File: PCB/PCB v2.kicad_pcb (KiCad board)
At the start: 4 copper layers, 56 x 45 mm, 132 parts, among them J2 USB_C_Receptacle_PowerOnly_6P, J3 6871XX182122_687110182122, J5 Conn_01x03_Pin, J7 Conn_02x06_Odd_Even, U1 TPD2E2U06DCK, U11 OPA4350EA_250, U12 OPA4350EA_250, U13 OPA4350EA_250, U2 ADS131M08xPBS, U3 74LVC1G17, U4 LM27762, U6 OPA4350EA_250, U7 LP5907MFX-3.3

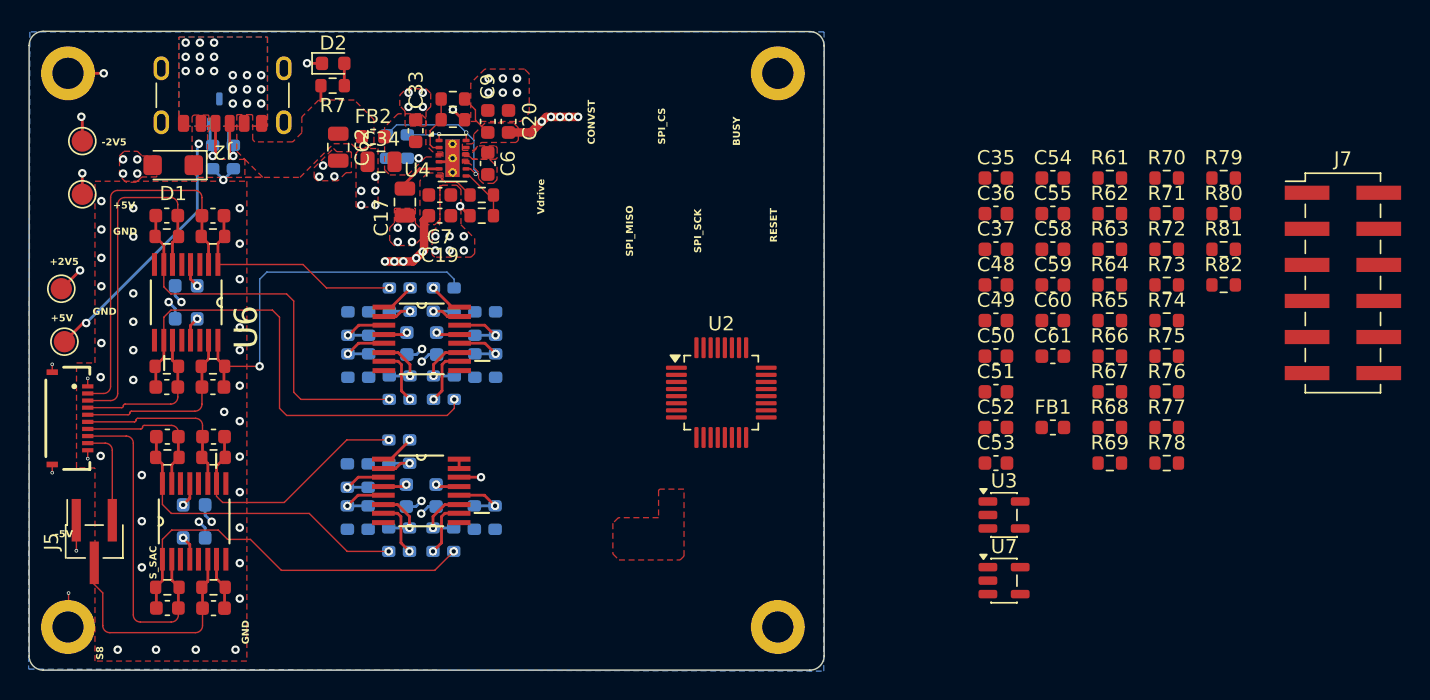
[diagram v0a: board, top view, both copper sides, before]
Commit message: Place U2, J7 and the ADC input dividers in a staggered two-column block
Placed in pcbnew:
- U2 (ADS131M08) at (166.74, 102.07).
- J7 (MCU header) at (165.03, 87.18), rotated -90.
- The Vout1 divider group, a vertical stack of C48 / R61 / R62 at
  x 156.08:
  - the 10 nF and the 1 kOhm to GND tie to the 1.1 kOhm's AIN pad;
  - the Vout pad sits between the two GND pads;
  - Vout1 is routed from U11, and the AIN0P spine is in place.

The other seven groups (R63-R76, C49-C55) copy that group shape exactly.
Eight 3.9 mm stacks in one column would need about 35 mm, and only
about 28 mm is free between J7 and the bottom edge. So they sit in two
columns, staggered by half a pitch:
- Column A at x 156.08: R61, R65, R69, R73 (AIN0/2/4/6).
- Column B at x 159.28: R63, R67, R71, R75 (AIN1/3/5/7).
- Group pitch is 4.7 mm, and column B is offset by 2.35 mm.

How the stagger works:
- Each column-B Vout enters straight through a gap in column A, between
  two GND pads.
- Each column-A AIN output leaves straight through a gap in column B.
- The groups run top to bottom in AIN0-7 order, so the fan-in to U2's
  top, left and bottom pins has no crossings.
- The block spans x 154.8-160.5 and y 91.9-112.2, leaving about 2.3 mm
  to U2's left pins.

Each group's AIN connections are routed like the Vout1 group
(0.1 mm, F.Cu).

DRC:
- Unconnected items 117 -> 103.
- No copper or courtyard violations added. The C48/J7 courtyard overlap
  comes from the manual placement.
- 40 new silkscreen reference overlaps, because the block is dense; this
  is cosmetic.

Still open: the GND pads of the divider block are not connected yet
(needs vias or an F.Cu GND pour).

Co-Authored-By: Claude Opus 5.5 <noreply@anthropic.com>
Claude-Session: https://claude.ai/code/session_01FkMyFfAWNWvsXoQ2tBz5gZ
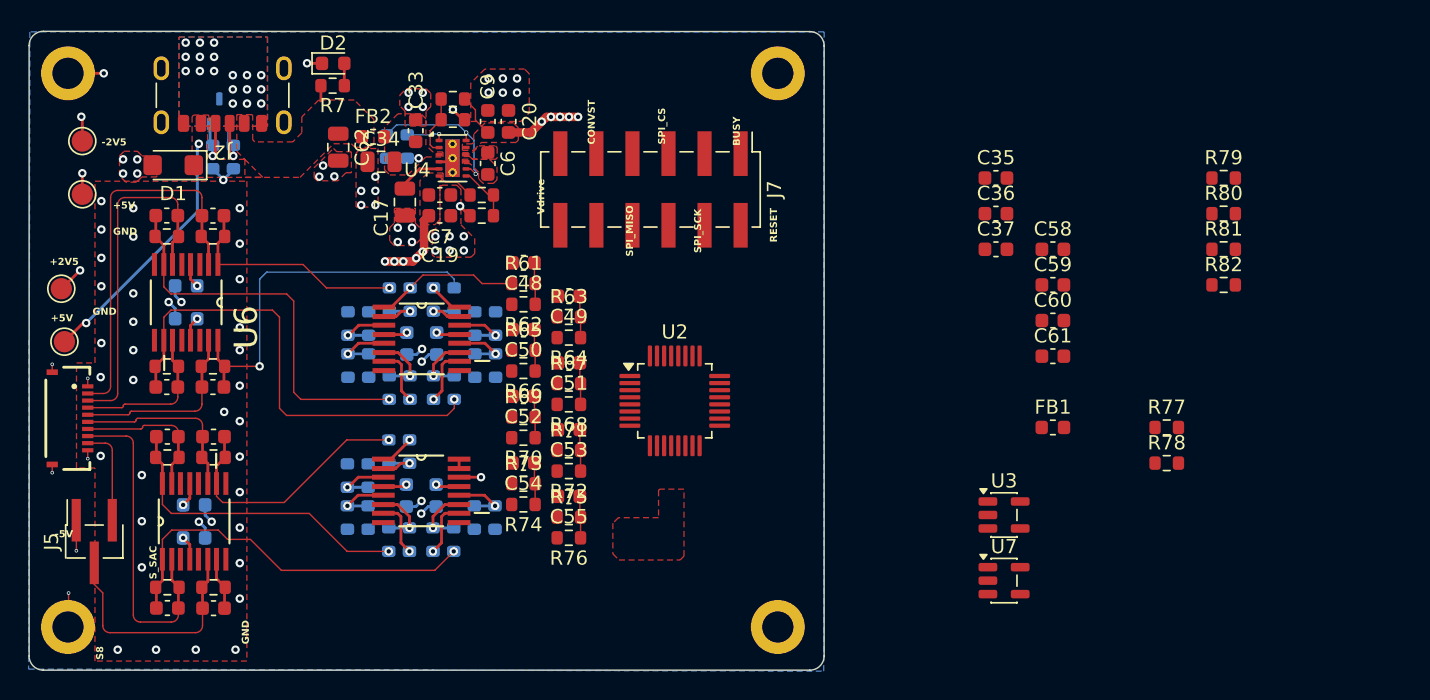
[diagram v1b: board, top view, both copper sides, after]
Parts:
- moved J7 49.2 mm to (165.0, 87.2), turned to -90 degrees
- moved R70 48.9 mm to (156.1, 104.7), turned to 180 degrees
- moved R73 47.4 mm to (156.1, 107.9)
- moved R74 47.1 mm to (156.1, 109.4), turned to 180 degrees
- moved R71 45.3 mm to (159.3, 105.6)
- moved R72 44.9 mm to (159.3, 107.0), turned to 180 degrees
- moved R75 43.6 mm to (159.3, 110.3)
- moved R76 43.4 mm to (159.3, 111.7), turned to 180 degrees
- moved C54 42.4 mm to (156.1, 106.4), turned to 180 degrees
- moved R61 42.0 mm to (156.1, 93.8)
- moved R62 41.8 mm to (156.1, 95.3), turned to 180 degrees
- moved R69 41.4 mm to (156.1, 103.2)
- moved R65 41.4 mm to (156.1, 98.5)
- moved R66 41.3 mm to (156.1, 100.0), turned to 180 degrees
- moved C55 39.5 mm to (159.3, 108.8), turned to 180 degrees
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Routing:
- net Vout1: track 2.43 -> 10.2 mm
- net /POWER SUPPLY - ADC - SACRIFIED SENSOR/AIN0P: track 0.00 -> 2.95 mm
- net /POWER SUPPLY - ADC - SACRIFIED SENSOR/AIN6P: track 0.00 -> 2.93 mm
- net /POWER SUPPLY - ADC - SACRIFIED SENSOR/AIN1P: track 0.00 -> 2.93 mm
- net /POWER SUPPLY - ADC - SACRIFIED SENSOR/AIN7P: track 0.00 -> 2.92 mm
- net /POWER SUPPLY - ADC - SACRIFIED SENSOR/AIN5P: track 0.00 -> 2.92 mm
- net /POWER SUPPLY - ADC - SACRIFIED SENSOR/AIN4P: track 0.00 -> 2.92 mm
- net /POWER SUPPLY - ADC - SACRIFIED SENSOR/AIN3P: track 0.00 -> 2.92 mm
- net /POWER SUPPLY - ADC - SACRIFIED SENSOR/AIN2P: track 0.00 -> 2.92 mm

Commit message: Route the ADC fan-in and Vout5-Vout7 to their dividers
AIN0P-AIN7P fan-in (routed in pcbnew, 0.1 mm, F.Cu):
- Each group's AIN spine runs to its U2 pin with no crossings.
- AIN0/1 go to the top pins, AIN2-5 to the left side, AIN6/7 to the
  bottom.

U12 outputs (0.1 mm; the mapping matches the schematic):
- Vout5 -> R69 (AIN4): F.Cu from its via at U12's top-left, over the top
  of U12, into the group. No new via.
- Vout6 -> R71 (AIN5): its via sits between Q6 and Q7, so it cannot
  escape on F.Cu.
  - It goes down on B.Cu, along y 114.0 under U12, and up at x 155.5.
  - It then comes up through a via at (154.4, 105.56) and runs on F.Cu
    through the R70/C54 gap in column A.
- Vout7 -> R73 (AIN6): the D7P fan-out via and trace, and U12's pin-13
  GND via, block it from going up on F.Cu.
  - It takes a B.Cu loop inside Vout6's (y 113.39, x 154.9).
  - It then comes up through a via at (154.3, 107.91) with a 1 mm stub
    to the pad.
- The loops run on B.Cu below the In1 GND plane and carry low-impedance
  op-amp outputs, so coupling does not matter.

The F.Cu corridor at y 110.26, below column A, is left free for Vsac ->
R75 (AIN7), to be routed with the Vsac bus.

DRC (trial, then re-checked on the saved board): unconnected items
95 -> 92, with no new violations.

Co-Authored-By: Claude Opus 5.5 <noreply@anthropic.com>
Claude-Session: https://claude.ai/code/session_01FkMyFfAWNWvsXoQ2tBz5gZ
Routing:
- net Vout6: track 4.03 -> 25.2 mm, vias 1 -> 2
- net /POWER SUPPLY - ADC - SACRIFIED SENSOR/AIN0P: track 2.95 -> 16.4 mm
- net Vout7: track 4.03 -> 15.8 mm, vias 1 -> 2
- net /POWER SUPPLY - ADC - SACRIFIED SENSOR/AIN7P: track 2.92 -> 13.1 mm
- net /POWER SUPPLY - ADC - SACRIFIED SENSOR/AIN6P: track 2.93 -> 13.0 mm
- net Vout5: track 2.43 -> 10.3 mm
- net /POWER SUPPLY - ADC - SACRIFIED SENSOR/AIN2P: track 2.92 -> 10.3 mm
- net /POWER SUPPLY - ADC - SACRIFIED SENSOR/AIN1P: track 2.93 -> 9.98 mm
- net /POWER SUPPLY - ADC - SACRIFIED SENSOR/AIN4P: track 2.92 -> 9.97 mm
- net /POWER SUPPLY - ADC - SACRIFIED SENSOR/AIN5P: track 2.92 -> 7.12 mm
- net /POWER SUPPLY - ADC - SACRIFIED SENSOR/AIN3P: track 2.92 -> 6.80 mm

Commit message: Rotate AIN1-AIN3 channel mapping and route Vout2-Vout4
Each U11 output can only leave the op-amp in one practical direction,
and that fixes the order the Vouts arrive at the divider block. Top to
bottom they arrive as Vout1, Vout4, Vout2, Vout3:
- Vout4 leaves pin 16 cleanly on F.Cu at the top.
- Vout3 can only go down and to the right from pin 10, because the D3P
  fan-out via blocks the way up.
- Vout2 is boxed in by the Q2/Q3 vias and must use B.Cu.

Keeping the old mapping would have cost 3-4 extra vias plus a 0.65 mm
squeeze that crosses an AIN line. The firmware has not been written yet,
so the rotation only costs a lookup table there.

Schematic (FOGLIO1): the three hierarchical labels at the divider inputs
are renamed. The names stay the set {Vout2, Vout3, Vout4}, so the sheet
pins and root global labels are untouched.
- R63 (AIN1P): Vout2 -> Vout4
- R65 (AIN2P): Vout3 -> Vout2
- R67 (AIN3P): Vout4 -> Vout3
The divider note on the sheet now carries the full map for the firmware:
  AIN0=Vout1 AIN1=Vout4 AIN2=Vout2 AIN3=Vout3
  AIN4=Vout5 AIN5=Vout6 AIN6=Vout7 AIN7=Vsac
Netlist: only those three nets change. ERC is 0 errors with the same 31
warnings. CHANGELOG Part 7 has the details.

PCB (after Update PCB from Schematic; 0.1 mm):
- Vout4 -> R63: F.Cu from U11 pin 16, between the pins and the D4P
  fan-out, through the R62/C50 gap at y 96.16. No via.
- Vout3 -> R67: F.Cu from pin 10, down and to the right at 45 degrees,
  clear of the D3P via, through the R66/C52 gap at y 100.86. No via.
- Vout2 -> R65: B.Cu from its fan-out via at R29, along y 102.9 below
  U11's bottom resistor row, up at x 155.26, into a via-in-pad at R65.

DRC (trial with the nets swapped on a copy, then re-checked on the saved
board): unconnected items 92 -> 89, with no new violations. Vout1-7 are
now all connected; only Vsac -> R75 remains.

Co-Authored-By: Claude Opus 5.5 <noreply@anthropic.com>
Claude-Session: https://claude.ai/code/session_01FkMyFfAWNWvsXoQ2tBz5gZ
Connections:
- R63 pad 1: Vout2 -> Vout4
- R65 pad 1: Vout3 -> Vout2
- R67 pad 1: Vout4 -> Vout3
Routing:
- net Vout2: track 4.03 -> 16.1 mm, vias 1 -> 2
- net Vout3: track 4.03 -> 11.6 mm
- net Vout4: track 2.43 -> 9.58 mm
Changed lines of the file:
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@@
 			(layers "F.Cu" "F.Mask" "F.Paste")
 			(roundrect_rratio 0.25)
-			(net "Vout3")
+			(net "Vout2")
 			(pintype "passive")
 		)
@@
 			(layers "F.Cu" "F.Mask" "F.Paste")
 			(roundrect_rratio 0.25)
-			(net "Vout4")
+			(net "Vout3")
 			(pintype "passive")
 		)
@@
 			(layers "F.Cu" "F.Mask" "F.Paste")
 			(roundrect_rratio 0.25)
-			(net "Vout2")
+			(net "Vout4")
 			(pintype "passive")
 		)
@@
 			)
 		)
-		(property "Datasheet" ""
+		(property "Datasheet" "https://content.harwin.com/asset/83ac22db-c414-41b6-9c7c-31bf0ab91f55/DRG-02647-Technical-Drawing-Datasheet-M50-363-pdf.pdf"
 			(at 0 0 90)
 			(layer "F.Fab")
@@
 			)
 		)
+		(property "MPN" "M50-3630342"
+			(at 0 0 90)
+			(unlocked yes)
+			(layer "F.Fab")
+			(hide yes)
+			(effects
+				(font
+					(size 1 1)
+					(thickness 0.15)
+				)
+			)
+		)
+		(property "Manufacturer" "Harwin"
+			(at 0 0 90)
+			(unlocked yes)
+			(layer "F.Fab")
+			(hide yes)
+			(effects
+				(font
+					(size 1 1)
+					(thickness 0.15)
+				)
+			)
+		)
 		(property ki_fp_filters "Connector*:*_1x??_*")
 		(sheetname "/POWER SUPPLY - ADC - SACRIFIED SENSOR/")
@@
 		(net "Vout2")
 	)
+	(via
+		(at 155.255 98.51)
+		(size 0.6)
+		(drill 0.3)
+		(layers "F.Cu" "B.Cu")
+		(net "Vout2")
+	)
+	(segment
+		(start 155.255 102.145)
+		(end 155.255 98.51)
+		(width 0.1)
+		(layer "B.Cu")
+		(net "Vout2")
+	)
+	(segment
+		(start 154.5 102.9)
+		(end 155.255 102.145)
+		(width 0.1)
+		(layer "B.Cu")
+		(net "Vout2")
+	)
+	(segment
+		(start 148.090347 101.9666)
+		(end 148.090347 102.9)
+		(width 0.1)
+		(layer "B.Cu")
+		(net "Vout2")
+	)
+	(segment
+		(start 148.090347 102.9)
+		(end 154.5 102.9)
+		(width 0.1)
+		(layer "B.Cu")
+		(net "Vout2")
+	)
+	(segment
+		(start 151.586 99.2814)
+		(end 152.7 99.2814)
+		(width 0.1)
+		(layer "F.Cu")
+		(net "Vout3")
+	)
 	(segment
 		(start 150.3477 99.5196)
@@
 	)
 	(segment
+		(start 152.7 99.2814)
+		(end 154.2786 100.86)
+		(width 0.1)
+		(layer "F.Cu")
+		(net "Vout3")
+	)
+	(segment
+		(start 154.2786 100.86)
+		(end 158.455 100.86)
+		(width 0.1)
+		(layer "F.Cu")
+		(net "Vout3")
+	)
+	(segment
 		(start 150.3477 101.3666)
 		(end 149.7477 101.9666)
@@
 	)
 	(segment
+		(start 153.5 95.4714)
+		(end 154.1886 96.16)
+		(width 0.1)
+		(layer "F.Cu")
+		(net "Vout4")
+	)
+	(segment
+		(start 154.1886 96.16)
+		(end 158.455 96.16)
+		(width 0.1)
+		(layer "F.Cu")
+		(net "Vout4")
+	)
+	(segment
 		(start 149.739 94.1116)
 		(end 149.739 94.1466)
@@
 		(layer "F.Cu")
 		(net "Vout4")
+	)
+	(segment
+		(start 151.586 95.4714)
+		(end 153.5 95.4714)
+		(width 0.1)
+		(layer "F.Cu")
+		(net "Vout4")

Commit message: Route the Vsac bus to the diff-amp +IN legs and the AIN7 divider
Vsac, the sacrificial-sensor charge-amp output (U13 section B), is the
reference each difference amplifier subtracts: Vout = 2*(Vsac - Qn).
It feeds seven +IN legs (R25/R30/R33/R35 on U11, R43/R45/R55 on U12;
4.99k + 10k to GND each) and the R75/R76/C55 divider to AIN7. That is
about 1.07 kOhm in total, roughly 2.3 mA at full scale.

Tap point: C8 pin 2. The net runs pin 7 -> R10 pin 2 -> C8 pin 2, and
the op-amp regulates its output where R10/C8 tie in. Tapping at C8 keeps
the bus current's IR drop inside the feedback loop, and it is also the
side the route leaves the guard on.

Route (0.1 mm, 4 vias):
- F.Cu: from C8 pin 2 along y 116.675, out of the guard, along the empty
  bottom strip to x 153.5, then up and along y 110.26 into R75 (AIN7).
  That corridor under the divider block was kept free for it.
- B.Cu trunk: via at (141.5, 116.675), then a vertical run at x 141.5,
  left of both diff-amp groups. Branches go into R25 (from above), R30
  (from below), R45 (from above) and R43 (from below).
- R33: B.Cu branch along y 103.7, in the gap between Vout2's B.Cu route
  and U12's top resistor row. It goes around the outside of Vout2 at
  x 156 and drops into R33 from above (y 94.9).
- R35: its pad is boxed in on B.Cu by Vout2 (y 102.9 / x 155.26). It is
  reached by an F.Cu hop: a via at the y 103.7 junction (151.3), then a
  via in the pocket at (152.66, 101.6), then a 1 mm B.Cu stub.
- R55: a short F.Cu spur off the x 153.5 run, with a via at
  (152.62, 112.2) just below the pad.

Why not all on B.Cu: a first version linked R33 to R35 inside U11's
group, and fed R55 from the y 103.7 corridor, both on B.Cu. DRC showed
these closed rings around the resistor groups. That cut the B.Cu -2V5
pour feeding the C24/C26 decoupling caps, and with it each op-amp's V-
pin. Trial runs with each branch alone and in pairs isolated the rings,
and they were replaced by the F.Cu hops above.

Corners rounded in pcbnew 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
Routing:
- net /POWER SUPPLY - ADC - SACRIFIED SENSOR/Vsac: track 3.72 -> 105.2 mm, vias 0 -> 4

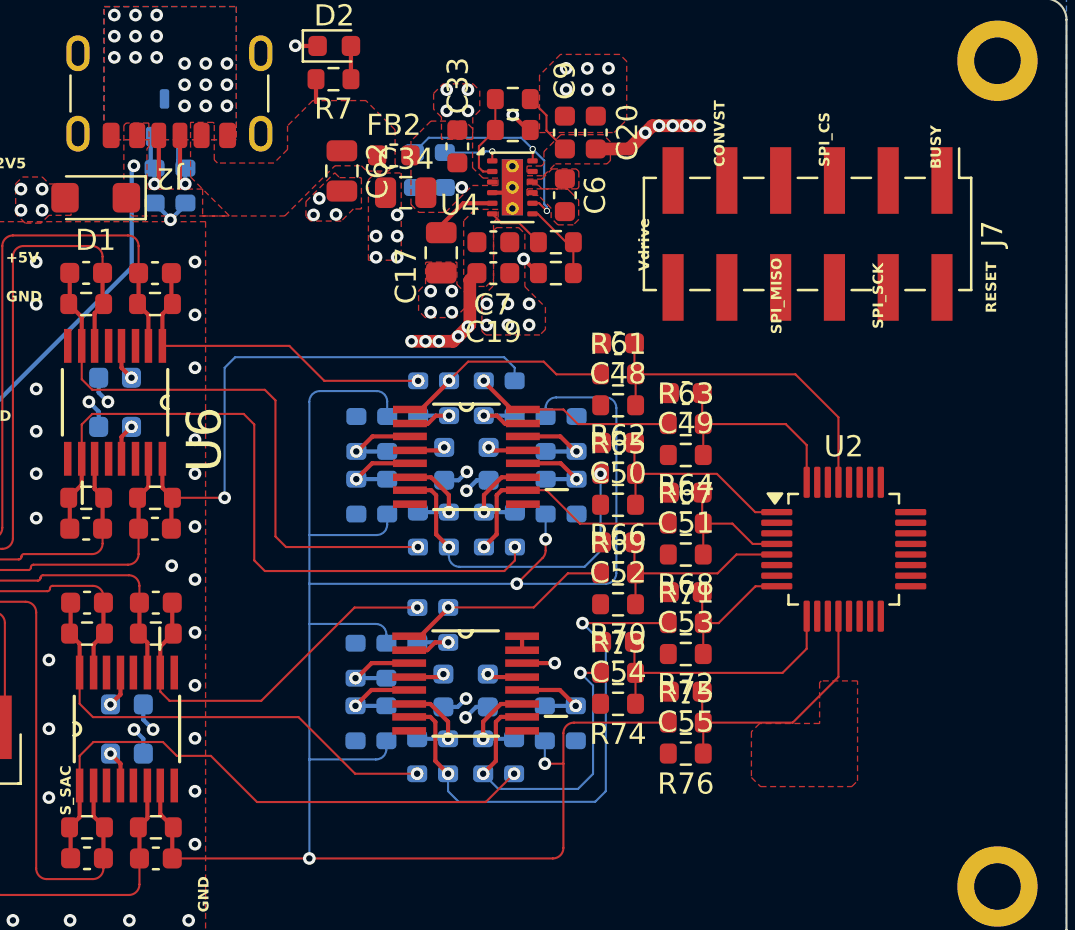
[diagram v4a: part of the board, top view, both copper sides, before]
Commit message: Ground the analog front end and J7 to the In1 GND plane
In1 is a solid GND plane. This adds 28 vias giving every GND pad in the
analog section, and J7's GND pins, a direct path to it.

Divider block (16 GND pads of the AIN0-7 anti-alias groups):
- The block is packed on purpose. Column B's GND pads face the 0.75 mm
  channel between the columns, and every gap in it carries an AIN or
  Vout trace. So via-in-pad is used (board is hand-soldered, so no
  wicking concern).
- Via in the pad: C49 R64 C51 R68 C53 R72 C55 R76 (column B), and
  C48 C50 R70 R74 (column A).
- C52 and C54 sit over a B.Cu Vout route, so their via is just to the
  left with a short F.Cu stub.
- R62/R34 and R66/R36 share one via each, between the F.Cu divider pad
  and the B.Cu diff-amp GND pad directly under it.

Diff-amp +IN legs (B.Cu): via in the pad for R26, R31, R46, R44, R56.
The C23/C24 and C25/C26 decoupling caps were already grounded through
the vias under U11 and U12.

U13 pins 5 and 12 (grounded +IN of sections B/C): Q6 and Q7 run through
U13's centre channel between these pins and the existing centre GND
vias. Each pin gets its own via next to it, which also lands on the
C27/C28 GND pads on B.Cu.

J7 (MCU header), digital return: vias past the outer end of pins 1, 3,
6 and 12 (0.3 mm stubs). Pin 11's via goes to the left of the pad,
because the +2V5 via row sits just past its end.

Vout6: the R74 via has to sit above the gap between the Vout6 and Vout7
B.Cu verticals, and that gap was 0.1 mm too narrow. Vout6's vertical
moves from x 155.5 to x 156.05 (same topology), leaving 0.225 mm each
side of the via.

DRC (trial on a snapshot, then on the saved board): unconnected items
81 -> 51, with no new violations. The first trial caught the J7 pin 11
via on the +2V5 via row; it was moved before applying.

Still open (22 GND items, all in the ADC area): U2's GND pins (AINxN,
power/ground pins) and the ADC support parts still off-board (C35-37,
C58-61, U7, U3, R79). To be done together with th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
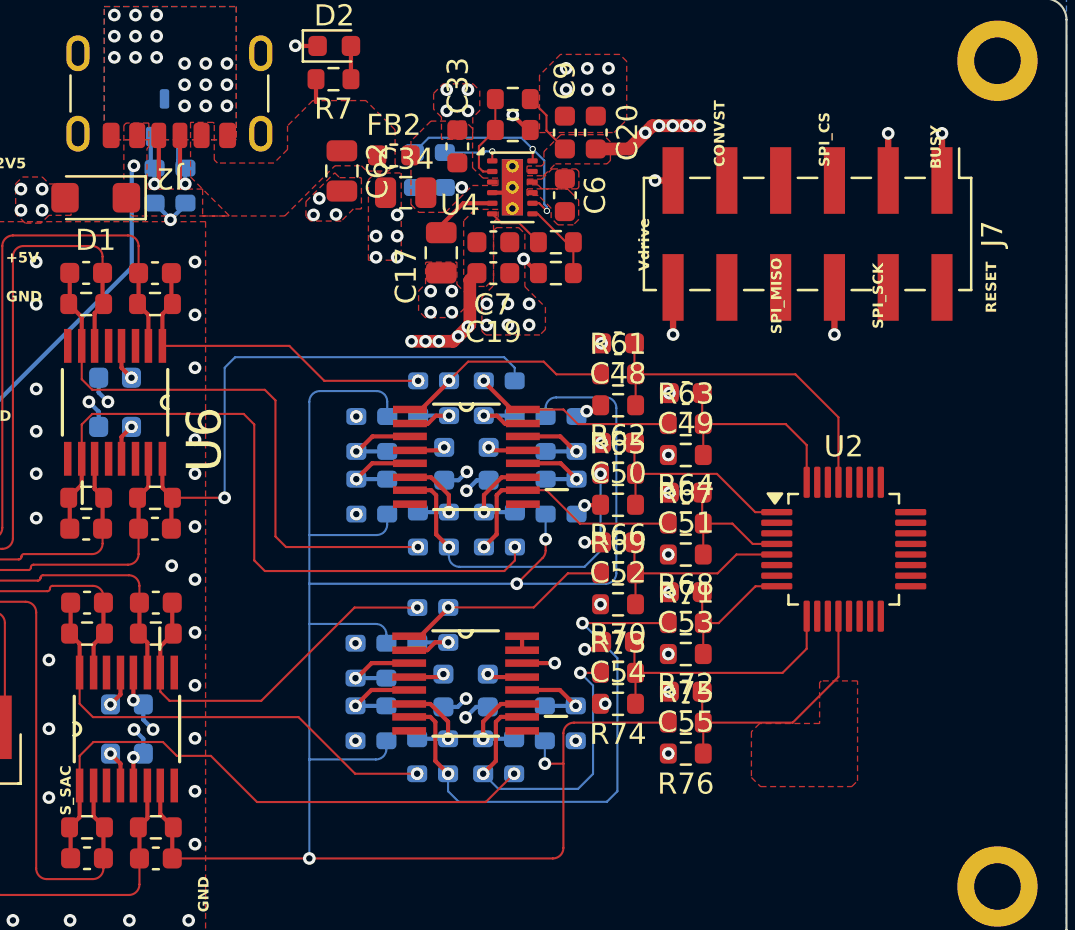
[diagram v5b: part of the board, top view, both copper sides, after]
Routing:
- net GND: track 27.3 -> 42.1 mm, vias 104 -> 132
- net Vout6: track 25.2 -> 25.9 mm
